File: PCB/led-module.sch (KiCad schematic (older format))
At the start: 11 parts, among them J3 CONN_PWR, U1 TLC5940NT, U2 TLC5940NT

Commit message: WIP
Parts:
- removed J_OUT1: CONN_02X04, Connectors:IDC_Header_Straight_8pins, symbol CONN_02X03
- J_IN1: value CONN_02X04 -> CONN_IF; footprint Connectors:IDC_Header_Straight_8pins -> Connectors:IDC_Header_Straight_10pins; symbol CONN_02X03 -> CONN_02X05
- L1, L2, L3, L4: footprint Displays_7-Segment:7SegmentLED_SBC18-11EGWA -> footprint:KYX-23101BS; Title (none) -> Valueasd
- R1, R2: footprint Resistors_THT:R_Axial_DIN0207_L6.3mm_D2.5mm_P7.62mm_Horizontal -> Resistors_THT:R_Axial_DIN0207_L6.3mm_D2.5mm_P10.16mm_Horizontal
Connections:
- net SOUT: now also J_IN1.6 (P6)
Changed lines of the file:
@@
 LIBS:valves
 LIBS:kyx-23101bs
+LIBS:switches
 LIBS:PCB-cache
 EELAYER 25 0
@@
 F 0 "L2" H 4350 2850 60  0000 C CNN
 F 1 "KYX-23101BS" V 4600 2250 60  0000 C CNN
-F 2 "Displays_7-Segment:7SegmentLED_SBC18-11EGWA" H 4300 2150 60  0001 C CNN
+F 2 "footprint:KYX-23101BS" H 4300 2150 60  0001 C CNN
 F 3 "" H 4300 2150 60  0001 C CNN
+F 4 "Valueasd" H 4300 2150 60  0001 C CNN "Title"
 	1    4300 2150
 	1    0    0    -1
@@
 F 0 "L1" H 2450 2850 60  0000 C CNN
 F 1 "KYX-23101BS" V 2700 2250 60  0000 C CNN
-F 2 "Displays_7-Segment:7SegmentLED_SBC18-11EGWA" H 2400 2150 60  0001 C CNN
+F 2 "footprint:KYX-23101BS" H 2400 2150 60  0001 C CNN
 F 3 "" H 2400 2150 60  0001 C CNN
+F 4 "Valueasd" H 2400 2150 60  0001 C CNN "Title"
 	1    2400 2150
 	1    0    0    -1
@@
 2SEG_G
 $Comp
-L Earth #PWR11
+L Earth #PWR08
 U 1 1 58DBB530
 P 3650 4250
-F 0 "#PWR11" H 3650 4000 50  0001 C CNN
+F 0 "#PWR08" H 3650 4000 50  0001 C CNN
 F 1 "Earth" H 3650 4100 50  0001 C CNN
 F 2 "" H 3650 4250 50  0001 C CNN
@@
 F 0 "L4" H 8200 2850 60  0000 C CNN
 F 1 "KYX-23101BS" V 8450 2250 60  0000 C CNN
-F 2 "Displays_7-Segment:7SegmentLED_SBC18-11EGWA" H 8150 2150 60  0001 C CNN
+F 2 "footprint:KYX-23101BS" H 8150 2150 60  0001 C CNN
 F 3 "" H 8150 2150 60  0001 C CNN
+F 4 "Valueasd" H 8150 2150 60  0001 C CNN "Title"
 	1    8150 2150
 	1    0    0    -1
@@
 F 0 "L3" H 6300 2850 60  0000 C CNN
 F 1 "KYX-23101BS" V 6550 2250 60  0000 C CNN
-F 2 "Displays_7-Segment:7SegmentLED_SBC18-11EGWA" H 6250 2150 60  0001 C CNN
+F 2 "footprint:KYX-23101BS" H 6250 2150 60  0001 C CNN
 F 3 "" H 6250 2150 60  0001 C CNN
+F 4 "Valueasd" H 6250 2150 60  0001 C CNN "Title"
 	1    6250 2150
 	1    0    0    -1
@@
 4SEG_G
 $Comp
-L Earth #PWR15
+L Earth #PWR09
 U 1 1 58DBBE8E
 P 7500 4250
-F 0 "#PWR15" H 7500 4000 50  0001 C CNN
+F 0 "#PWR09" H 7500 4000 50  0001 C CNN
 F 1 "Earth" H 7500 4100 50  0001 C CNN
 F 2 "" H 7500 4250 50  0001 C CNN
@@
 VCC
 $Comp
-L Earth #PWR8
+L Earth #PWR010
 U 1 1 58DBC2BB
 P 1750 4800
-F 0 "#PWR8" H 1750 4550 50  0001 C CNN
+F 0 "#PWR010" H 1750 4550 50  0001 C CNN
 F 1 "Earth" H 1750 4650 50  0001 C CNN
 F 2 "" H 1750 4800 50  0001 C CNN
@@
 $EndComp
 $Comp
-L Earth #PWR10
+L Earth #PWR011
 U 1 1 58DBC2D8
 P 1950 4800
-F 0 "#PWR10" H 1950 4550 50  0001 C CNN
+F 0 "#PWR011" H 1950 4550 50  0001 C CNN
 F 1 "Earth" H 1950 4650 50  0001 C CNN
 F 2 "" H 1950 4800 50  0001 C CNN
@@
 F 0 "R1" V 1930 5100 50  0000 C CNN
 F 1 "2k" V 1850 5100 50  0000 C CNN
-F 2 "Resistors_THT:R_Axial_DIN0207_L6.3mm_D2.5mm_P7.62mm_Horizontal" V 1780 5100 50  0001 C CNN
+F 2 "Resistors_THT:R_Axial_DIN0207_L6.3mm_D2.5mm_P10.16mm_Horizontal" V 1780 5100 50  0001 C CNN
 F 3 "" H 1850 5100 50  0001 C CNN
 	1    1850 5100
@@
 F 0 "R2" V 5780 5300 50  0000 C CNN
 F 1 "2k" V 5700 5300 50  0000 C CNN
-F 2 "Resistors_THT:R_Axial_DIN0207_L6.3mm_D2.5mm_P7.62mm_Horizontal" V 5630 5300 50  0001 C CNN
+F 2 "Resistors_THT:R_Axial_DIN0207_L6.3mm_D2.5mm_P10.16mm_Horizontal" V 5630 5300 50  0001 C CNN
 F 3 "" H 5700 5300 50  0001 C CNN
 	1    5700 5300
@@
 $EndComp
 $Comp
-L Earth #PWR9
+L Earth #PWR012
 U 1 1 58DBC5EF
 P 1850 5250
-F 0 "#PWR9" H 1850 5000 50  0001 C CNN
+F 0 "#PWR012" H 1850 5000 50  0001 C CNN
 F 1 "Earth" H 1850 5100 50  0001 C CNN
 F 2 "" H 1850 5250 50  0001 C CNN
@@
 $EndComp
 $Comp
-L Earth #PWR12
+L Earth #PWR013
 U 1 1 58DBC918
 P 5600 4800
-F 0 "#PWR12" H 5600 4550 50  0001 C CNN
+F 0 "#PWR013" H 5600 4550 50  0001 C CNN
 F 1 "Earth" H 5600 4650 50  0001 C CNN
 F 2 "" H 5600 4800 50  0001 C CNN
@@
 $EndComp
 $Comp
-L Earth #PWR14
+L Earth #PWR014
 U 1 1 58DBC93B
 P 5800 4800
-F 0 "#PWR14" H 5800 4550 50  0001 C CNN
+F 0 "#PWR014" H 5800 4550 50  0001 C CNN
 F 1 "Earth" H 5800 4650 50  0001 C CNN
 F 2 "" H 5800 4800 50  0001 C CNN
@@
 SCLK
 $Comp
-L Earth #PWR13
+L Earth #PWR015
 U 1 1 58DBCAE9
 P 5700 5450
-F 0 "#PWR13" H 5700 5200 50  0001 C CNN
+F 0 "#PWR015" H 5700 5200 50  0001 C CNN
 F 1 "Earth" H 5700 5300 50  0001 C CNN
 F 2 "" H 5700 5450 50  0001 C CNN
@@
 Wire Bus Line
 	7250 1750 7250 3050
-$Comp
-L CONN_02X03 J_OUT1
-U 1 1 58DBAF2A
-P 8850 4550
-F 0 "J_OUT1" H 8850 4750 50  0000 C CNN
-F 1 "CONN_02X04" H 8850 4350 50  0000 C CNN
-F 2 "Connectors:IDC_Header_Straight_8pins" H 8850 3350 50  0001 C CNN
-F 3 "" H 8850 3350 50  0001 C CNN
-F 4 "Valueasd" H 8850 4550 60  0001 C CNN "Title"
-	1    8850 4550
-	1    0    0    -1
-$EndComp
 Text HLabel 8700 5350 0    39   Input ~ 0
 VCC
 $Comp
-L Earth #PWR16
+L Earth #PWR016
 U 1 1 58DBB0DE
 P 8700 5250
-F 0 "#PWR16" H 8700 5000 50  0001 C CNN
+F 0 "#PWR016" H 8700 5000 50  0001 C CNN
 F 1 "Earth" H 8700 5100 50  0001 C CNN
 F 2 "" H 8700 5250 50  0001 C CNN
@@
 	0    1    1    0
 $EndComp
-Text HLabel 8600 4450 0    39   Input ~ 0
-SCLK
-Text HLabel 9100 4450 2    39   Input ~ 0
-XLAT
-Text HLabel 8600 4550 0    39   Input ~ 0
-BLANK
-Text HLabel 9100 4550 2    39   Input ~ 0
-GSCLK
-Text HLabel 8600 4650 0    39   Output ~ 0
-SOUT
 Text HLabel 3650 1500 1    39   Input ~ 0
 VLED
@@
 $EndComp
 $Comp
-L CONN_02X03 J_IN1
+L CONN_02X05 J_IN1
 U 1 1 58DE4F42
-P 8850 4000
-F 0 "J_IN1" H 8850 4200 50  0000 C CNN
-F 1 "CONN_02X04" H 8850 3800 50  0000 C CNN
-F 2 "Connectors:IDC_Header_Straight_8pins" H 8850 2800 50  0001 C CNN
-F 3 "" H 8850 2800 50  0001 C CNN
-F 4 "Valueasd" H 8850 4000 60  0001 C CNN "Title"
-	1    8850 4000
+P 8850 4100
+F 0 "J_IN1" H 8850 4400 50  0000 C CNN
+F 1 "CONN_IF" H 8850 3800 50  0000 C CNN
+F 2 "Connectors:IDC_Header_Straight_10pins" H 8850 2900 50  0001 C CNN
+F 3 "" H 8850 2900 50  0001 C CNN
+F 4 "Valueasd" H 8850 4100 60  0001 C CNN "Title"
+	1    8850 4100
 	1    0    0    -1
 $EndComp
@@
 Text HLabel 8600 4100 0    39   Input ~ 0
 SIN
+Text HLabel 9100 4100 2    39   Output ~ 0
+SOUT
 $EndSCHEMATC

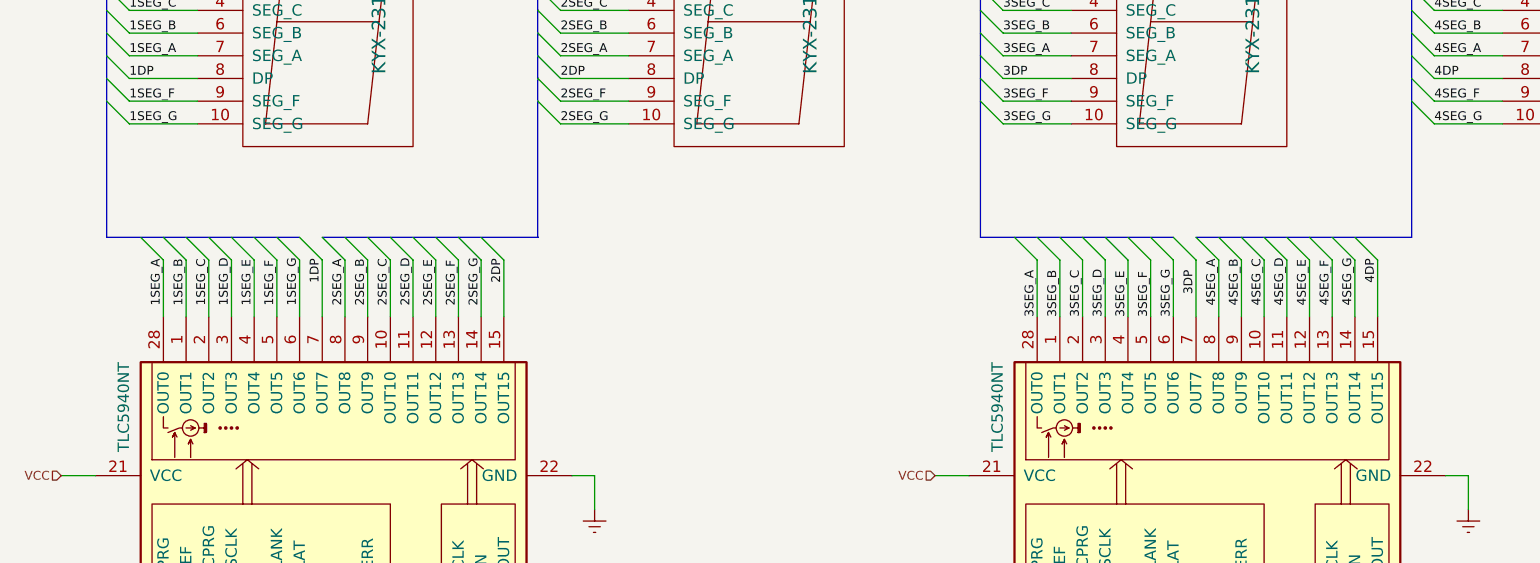
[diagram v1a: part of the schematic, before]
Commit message: Перегруппировка коннекторов модуля
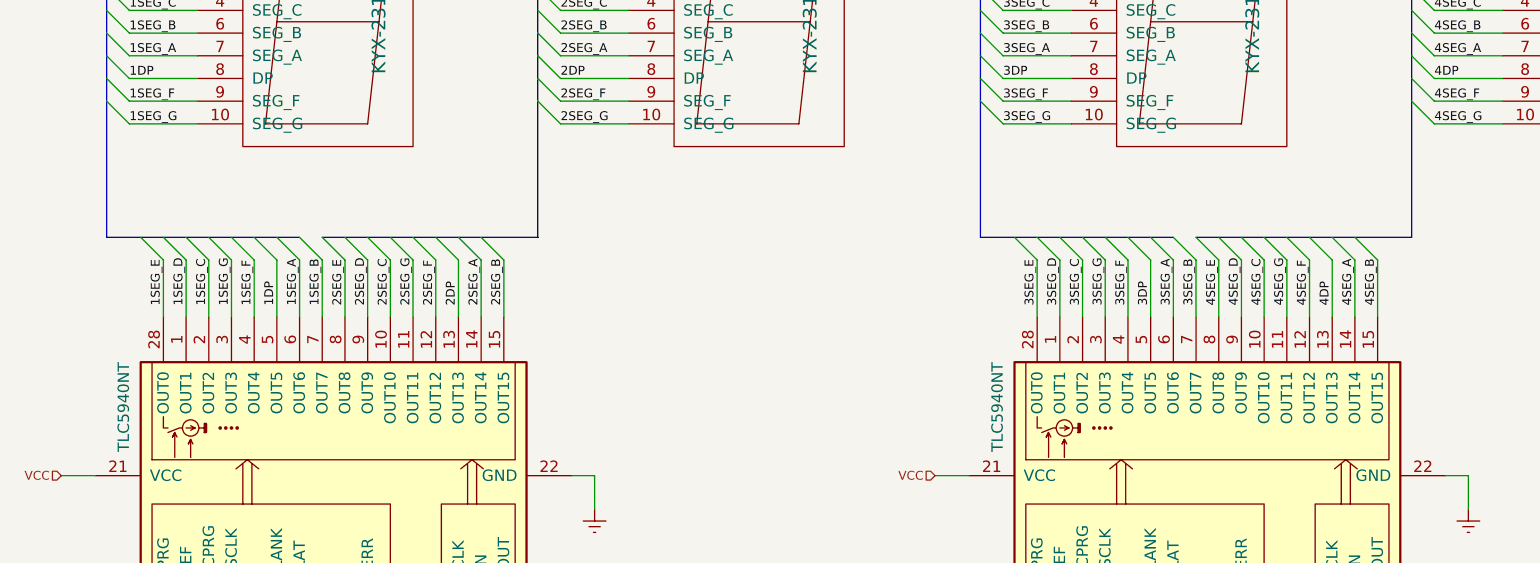
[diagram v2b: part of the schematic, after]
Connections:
- net 1DP: now also U1.5 (OUT5); no longer U1.7 (OUT7)
- net 1SEG_A: now also U1.6 (OUT6); no longer U1.28 (OUT0)
- net 1SEG_B: now also U1.7 (OUT7); no longer U1.1 (OUT1)
- net 1SEG_D: now also U1.1 (OUT1); no longer U1.3 (OUT3)
- net 1SEG_E: now also U1.28 (OUT0); no longer U1.4 (OUT4)
- net 1SEG_F: now also U1.4 (OUT4); no longer U1.5 (OUT5)
- net 1SEG_G: now also U1.3 (OUT3); no longer U1.6 (OUT6)
- net 2DP: now also U1.13 (OUT13); no longer U1.15 (OUT15)
- net 2SEG_A: now also U1.14 (OUT14); no longer U1.8 (OUT8)
- net 2SEG_B: now also U1.15 (OUT15); no longer U1.9 (OUT9)
- net 2SEG_D: now also U1.9 (OUT9); no longer U1.11 (OUT11)
- net 2SEG_E: now also U1.8 (OUT8); no longer U1.12 (OUT12)
- net 2SEG_F: now also U1.12 (OUT12); no longer U1.13 (OUT13)
- net 2SEG_G: now also U1.11 (OUT11); no longer U1.14 (OUT14)
- net 3DP: now also U2.5 (OUT5); no longer U2.7 (OUT7)
- net 3SEG_A: now also U2.6 (OUT6); no longer U2.28 (OUT0)
- net 3SEG_B: now also U2.7 (OUT7); no longer U2.1 (OUT1)
- net 3SEG_D: now also U2.1 (OUT1); no longer U2.3 (OUT3)
- net 3SEG_E: now also U2.28 (OUT0); no longer U2.4 (OUT4)
- net 3SEG_F: now also U2.4 (OUT4); no longer U2.5 (OUT5)
- net 3SEG_G: now also U2.3 (OUT3); no longer U2.6 (OUT6)
- net 4DP: now also U2.13 (OUT13); no longer U2.15 (OUT15)
- net 4SEG_A: now also U2.14 (OUT14); no longer U2.8 (OUT8)
- net 4SEG_B: now also U2.15 (OUT15); no longer U2.9 (OUT9)
- net 4SEG_D: now also U2.9 (OUT9); no longer U2.11 (OUT11)
- net 4SEG_E: now also U2.8 (OUT8); no longer U2.12 (OUT12)
- net 4SEG_F: now also U2.12 (OUT12); no longer U2.13 (OUT13)
- net 4SEG_G: now also U2.11 (OUT11); no longer U2.14 (OUT14)
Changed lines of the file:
@@
 1SEG_G
 Text Label 1750 3350 1    39   ~ 0
-1SEG_A
+1SEG_E
 Text Label 1850 3350 1    39   ~ 0
-1SEG_B
+1SEG_D
 Text Label 1950 3350 1    39   ~ 0
 1SEG_C
 Text Label 2050 3350 1    39   ~ 0
-1SEG_D
+1SEG_G
 Text Label 2150 3350 1    39   ~ 0
-1SEG_E
+1SEG_F
 Text Label 2250 3350 1    39   ~ 0
-1SEG_F
+1DP
 Text Label 2350 3350 1    39   ~ 0
-1SEG_G
-Text Label 2450 3250 1    39   ~ 0
-1DP
+1SEG_A
+Text Label 2450 3350 1    39   ~ 0
+1SEG_B
 Entry Wire Line
 	2450 3050 2550 3150
@@
 	3150 3050 3250 3150
 Text Label 2550 3350 1    39   ~ 0
-2SEG_A
+2SEG_E
 Text Label 2650 3350 1    39   ~ 0
-2SEG_B
+2SEG_D
 Text Label 2750 3350 1    39   ~ 0
 2SEG_C
 Text Label 2850 3350 1    39   ~ 0
-2SEG_D
+2SEG_G
 Text Label 2950 3350 1    39   ~ 0
-2SEG_E
+2SEG_F
 Text Label 3050 3350 1    39   ~ 0
-2SEG_F
+2DP
 Text Label 3150 3350 1    39   ~ 0
-2SEG_G
-Text Label 3250 3250 1    39   ~ 0
-2DP
+2SEG_A
+Text Label 3250 3350 1    39   ~ 0
+2SEG_B
 Entry Wire Line
 	3400 1750 3500 1850
@@
 Text Label 5450 2550 0    39   ~ 0
 3SEG_G
-Text Label 5600 3400 1    39   ~ 0
+Text Label 5600 3350 1    39   ~ 0
+3SEG_E
+Text Label 5700 3350 1    39   ~ 0
+3SEG_D
+Text Label 5800 3350 1    39   ~ 0
+3SEG_C
+Text Label 5900 3350 1    39   ~ 0
+3SEG_G
+Text Label 6000 3350 1    39   ~ 0
+3SEG_F
+Text Label 6100 3350 1    39   ~ 0
+3DP
+Text Label 6200 3350 1    39   ~ 0
 3SEG_A
-Text Label 5700 3400 1    39   ~ 0
+Text Label 6300 3350 1    39   ~ 0
 3SEG_B
-Text Label 5800 3400 1    39   ~ 0
-3SEG_C
-Text Label 5900 3400 1    39   ~ 0
-3SEG_D
-Text Label 6000 3400 1    39   ~ 0
-3SEG_E
-Text Label 6100 3400 1    39   ~ 0
-3SEG_F
-Text Label 6200 3400 1    39   ~ 0
-3SEG_G
-Text Label 6300 3300 1    39   ~ 0
-3DP
 Entry Wire Line
 	6300 3050 6400 3150
@@
 	7000 3050 7100 3150
 Text Label 6400 3350 1    39   ~ 0
-4SEG_A
+4SEG_E
 Text Label 6500 3350 1    39   ~ 0
-4SEG_B
+4SEG_D
 Text Label 6600 3350 1    39   ~ 0
 4SEG_C
 Text Label 6700 3350 1    39   ~ 0
-4SEG_D
+4SEG_G
 Text Label 6800 3350 1    39   ~ 0
-4SEG_E
+4SEG_F
 Text Label 6900 3350 1    39   ~ 0
-4SEG_F
+4DP
 Text Label 7000 3350 1    39   ~ 0
-4SEG_G
-Text Label 7100 3250 1    39   ~ 0
-4DP
+4SEG_A
+Text Label 7100 3350 1    39   ~ 0
+4SEG_B
 Entry Wire Line
 	7250 1750 7350 1850

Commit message: layoyt changed
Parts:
- removed L3, L4: KYX-23101BS, footprint:KYX-23101BS, symbol KYX-23101BS
- removed R2: 2k, Resistors_THT:R_Axial_DIN0207_L6.3mm_D2.5mm_P10.16mm_Horizontal, symbol R
- removed U2: TLC5940NT, Housings_DIP:DIP-28_W7.62mm, symbol TLC5940NT
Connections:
- net SOUT: now also U1.17 (SOUT)
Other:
- moved on the sheet: J3, J_IN1

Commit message: WIP
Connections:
- net BLANK: now also J_IN1.5 (P5); no longer J_IN1.3 (P3)
- net GSCLK: now also J_IN1.7 (P7); no longer J_IN1.4 (P4)
- net SIN: now also J_IN1.2 (P2); no longer J_IN1.5 (P5)
- net SOUT: now also J_IN1.9 (P9); no longer J_IN1.6 (P6)
- net XLAT: now also J_IN1.3 (P3); no longer J_IN1.2 (P2)
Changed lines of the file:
@@
 VLED
 $Comp
-L Earth #PWR010
+L Earth #PWR09
 U 1 1 58DBC2BB
 P 1750 4800
-F 0 "#PWR010" H 1750 4550 50  0001 C CNN
+F 0 "#PWR09" H 1750 4550 50  0001 C CNN
 F 1 "Earth" H 1750 4650 50  0001 C CNN
 F 2 "" H 1750 4800 50  0001 C CNN
@@
 $EndComp
 $Comp
-L Earth #PWR011
+L Earth #PWR010
 U 1 1 58DBC2D8
 P 1950 4800
-F 0 "#PWR011" H 1950 4550 50  0001 C CNN
+F 0 "#PWR010" H 1950 4550 50  0001 C CNN
 F 1 "Earth" H 1950 4650 50  0001 C CNN
 F 2 "" H 1950 4800 50  0001 C CNN
@@
 $EndComp
 $Comp
-L Earth #PWR012
+L Earth #PWR011
 U 1 1 58DBC5EF
 P 1850 5250
-F 0 "#PWR012" H 1850 5000 50  0001 C CNN
+F 0 "#PWR011" H 1850 5000 50  0001 C CNN
 F 1 "Earth" H 1850 5100 50  0001 C CNN
 F 2 "" H 1850 5250 50  0001 C CNN
@@
 	1900 1650 1750 1650
 Wire Wire Line
-	1750 1500 1750 1650
-Wire Wire Line
-	1750 1650 1750 1750
+	1750 1500 1750 1750
 Wire Wire Line
 	1750 1750 1900 1750
@@
 	3800 1650 3650 1650
 Wire Wire Line
-	3650 1500 3650 1650
-Wire Wire Line
-	3650 1650 3650 1750
+	3650 1500 3650 1750
 Wire Wire Line
 	3650 1750 3800 1750
@@
 	1850 4950 1850 4800
 Wire Bus Line
-	1500 3050 1650 3050
-Wire Bus Line
-	1650 3050 1750 3050
-Wire Bus Line
-	1750 3050 1850 3050
-Wire Bus Line
-	1850 3050 1950 3050
-Wire Bus Line
-	1950 3050 2050 3050
-Wire Bus Line
-	2050 3050 2150 3050
-Wire Bus Line
-	2150 3050 2250 3050
-Wire Bus Line
-	2250 3050 2350 3050
-Wire Bus Line
-	3400 3050 3150 3050
-Wire Bus Line
-	3150 3050 3050 3050
-Wire Bus Line
-	3050 3050 2950 3050
-Wire Bus Line
-	2950 3050 2850 3050
-Wire Bus Line
-	2850 3050 2750 3050
-Wire Bus Line
-	2750 3050 2650 3050
-Wire Bus Line
-	2650 3050 2550 3050
-Wire Bus Line
-	2550 3050 2450 3050
-Wire Bus Line
-	3400 1750 3400 1850
-Wire Bus Line
-	3400 1850 3400 1950
-Wire Bus Line
-	3400 1950 3400 2050
-Wire Bus Line
-	3400 2050 3400 2150
-Wire Bus Line
-	3400 2150 3400 2250
-Wire Bus Line
-	3400 2250 3400 2350
-Wire Bus Line
-	3400 2350 3400 2450
-Wire Bus Line
-	3400 2450 3400 3050
-Wire Bus Line
-	1500 1750 1500 1850
-Wire Bus Line
-	1500 1850 1500 1950
-Wire Bus Line
-	1500 1950 1500 2050
-Wire Bus Line
-	1500 2050 1500 2150
-Wire Bus Line
-	1500 2150 1500 2250
-Wire Bus Line
-	1500 2250 1500 2350
-Wire Bus Line
-	1500 2350 1500 2450
-Wire Bus Line
-	1500 2450 1500 3050
+	1500 3050 2350 3050
+Wire Bus Line
+	3400 3050 2450 3050
+Wire Bus Line
+	3400 1750 3400 3050
+Wire Bus Line
+	1500 1750 1500 3050
 Text HLabel 5850 4550 0    39   Input ~ 0
 VCC
 $Comp
-L Earth #PWR016
+L Earth #PWR012
 U 1 1 58DBB0DE
 P 5850 4450
-F 0 "#PWR016" H 5850 4200 50  0001 C CNN
+F 0 "#PWR012" H 5850 4200 50  0001 C CNN
 F 1 "Earth" H 5850 4300 50  0001 C CNN
 F 2 "" H 5850 4450 50  0001 C CNN
@@
 Text HLabel 5750 3100 0    39   Input ~ 0
 SCLK
+Text HLabel 5750 3200 0    39   Input ~ 0
+XLAT
+Text HLabel 5750 3300 0    39   Input ~ 0
+BLANK
+Text HLabel 5750 3400 0    39   Input ~ 0
+GSCLK
 Text HLabel 6250 3100 2    39   Input ~ 0
-XLAT
-Text HLabel 5750 3200 0    39   Input ~ 0
-BLANK
-Text HLabel 6250 3200 2    39   Input ~ 0
-GSCLK
-Text HLabel 5750 3300 0    39   Input ~ 0
 SIN
-Text HLabel 6250 3300 2    39   Output ~ 0
+Text HLabel 5750 3500 0    39   Output ~ 0
 SOUT
 Text HLabel 3150 4800 3    39   Input ~ 0

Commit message: KiCad 4.0.7 update
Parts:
- added RV1: 2K, Potentiometers:Potentiometer_Triwood_RM-065, symbol POT_TRIM
- R1: value 2k -> 1k
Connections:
- net Earth: now also RV1.2; no longer R1.2
- new net: R1.2, RV1.3
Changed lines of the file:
@@
 2SEG_G
 $Comp
-L Earth #PWR08
+L Earth #PWR011
 U 1 1 58DBB530
 P 3650 4250
-F 0 "#PWR08" H 3650 4000 50  0001 C CNN
+F 0 "#PWR011" H 3650 4000 50  0001 C CNN
 F 1 "Earth" H 3650 4100 50  0001 C CNN
 F 2 "" H 3650 4250 50  0001 C CNN
@@
 VLED
 $Comp
-L Earth #PWR09
+L Earth #PWR012
 U 1 1 58DBC2BB
 P 1750 4800
-F 0 "#PWR09" H 1750 4550 50  0001 C CNN
+F 0 "#PWR012" H 1750 4550 50  0001 C CNN
 F 1 "Earth" H 1750 4650 50  0001 C CNN
 F 2 "" H 1750 4800 50  0001 C CNN
@@
 $EndComp
 $Comp
-L Earth #PWR010
+L Earth #PWR013
 U 1 1 58DBC2D8
 P 1950 4800
-F 0 "#PWR010" H 1950 4550 50  0001 C CNN
+F 0 "#PWR013" H 1950 4550 50  0001 C CNN
 F 1 "Earth" H 1950 4650 50  0001 C CNN
 F 2 "" H 1950 4800 50  0001 C CNN
@@
 P 1850 5100
 F 0 "R1" V 1930 5100 50  0000 C CNN
-F 1 "2k" V 1850 5100 50  0000 C CNN
+F 1 "1k" V 1850 5100 50  0000 C CNN
 F 2 "Resistors_THT:R_Axial_DIN0207_L6.3mm_D2.5mm_P10.16mm_Horizontal" V 1780 5100 50  0001 C CNN
 F 3 "" H 1850 5100 50  0001 C CNN
@@
 $EndComp
 $Comp
-L Earth #PWR011
+L Earth #PWR014
 U 1 1 58DBC5EF
-P 1850 5250
-F 0 "#PWR011" H 1850 5000 50  0001 C CNN
-F 1 "Earth" H 1850 5100 50  0001 C CNN
-F 2 "" H 1850 5250 50  0001 C CNN
-F 3 "" H 1850 5250 50  0001 C CNN
-	1    1850 5250
-	1    0    0    -1
+P 1600 5450
+F 0 "#PWR014" H 1600 5200 50  0001 C CNN
+F 1 "Earth" H 1600 5300 50  0001 C CNN
+F 2 "" H 1600 5450 50  0001 C CNN
+F 3 "" H 1600 5450 50  0001 C CNN
+	1    1600 5450
+	0    1    1    0
 $EndComp
 Wire Wire Line
@@
 VCC
 $Comp
-L Earth #PWR012
+L Earth #PWR015
 U 1 1 58DBB0DE
 P 5850 4450
-F 0 "#PWR012" H 5850 4200 50  0001 C CNN
+F 0 "#PWR015" H 5850 4200 50  0001 C CNN
 F 1 "Earth" H 5850 4300 50  0001 C CNN
 F 2 "" H 5850 4450 50  0001 C CNN
@@
 Text HLabel 3250 4800 3    39   Input ~ 0
 SOUT
+$Comp
+L POT_TRIM RV1
+U 1 1 59B2864A
+P 1850 5450
+F 0 "RV1" V 1675 5450 50  0000 C CNN
+F 1 "2K" V 1750 5450 50  0000 C CNN
+F 2 "Potentiometers:Potentiometer_Triwood_RM-065" H 1850 5450 50  0001 C CNN
+F 3 "" H 1850 5450 50  0001 C CNN
+	1    1850 5450
+	-1   0    0    1
+$EndComp
+Wire Wire Line
+	1600 5450 1700 5450
+Wire Wire Line
+	1850 5300 1850 5250
 $EndSCHEMATC
